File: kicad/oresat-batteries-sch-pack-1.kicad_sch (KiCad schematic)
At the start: 79 parts, among them Q12 SI7625DN-T1-GE3, Q13 SI7625DN-T1-GE3, Q14 NTR4101, Q15 NTR4101, Q16 SI7625DN-T1-GE3, Q17 SI7625DN-T1-GE3, Q18 SI7625DN-T1-GE3, Q19 SI7625DN-T1-GE3, Q6 PM45VEN, Q7 PM45VEN, Q8 PM45VEN, Q9 PM45VEN, U10 LTC4412, U11 LTC4412, U12 MAX17205G, U8 S-8209AAA-T8T1U, U9 S-8209AAA-T8T1U

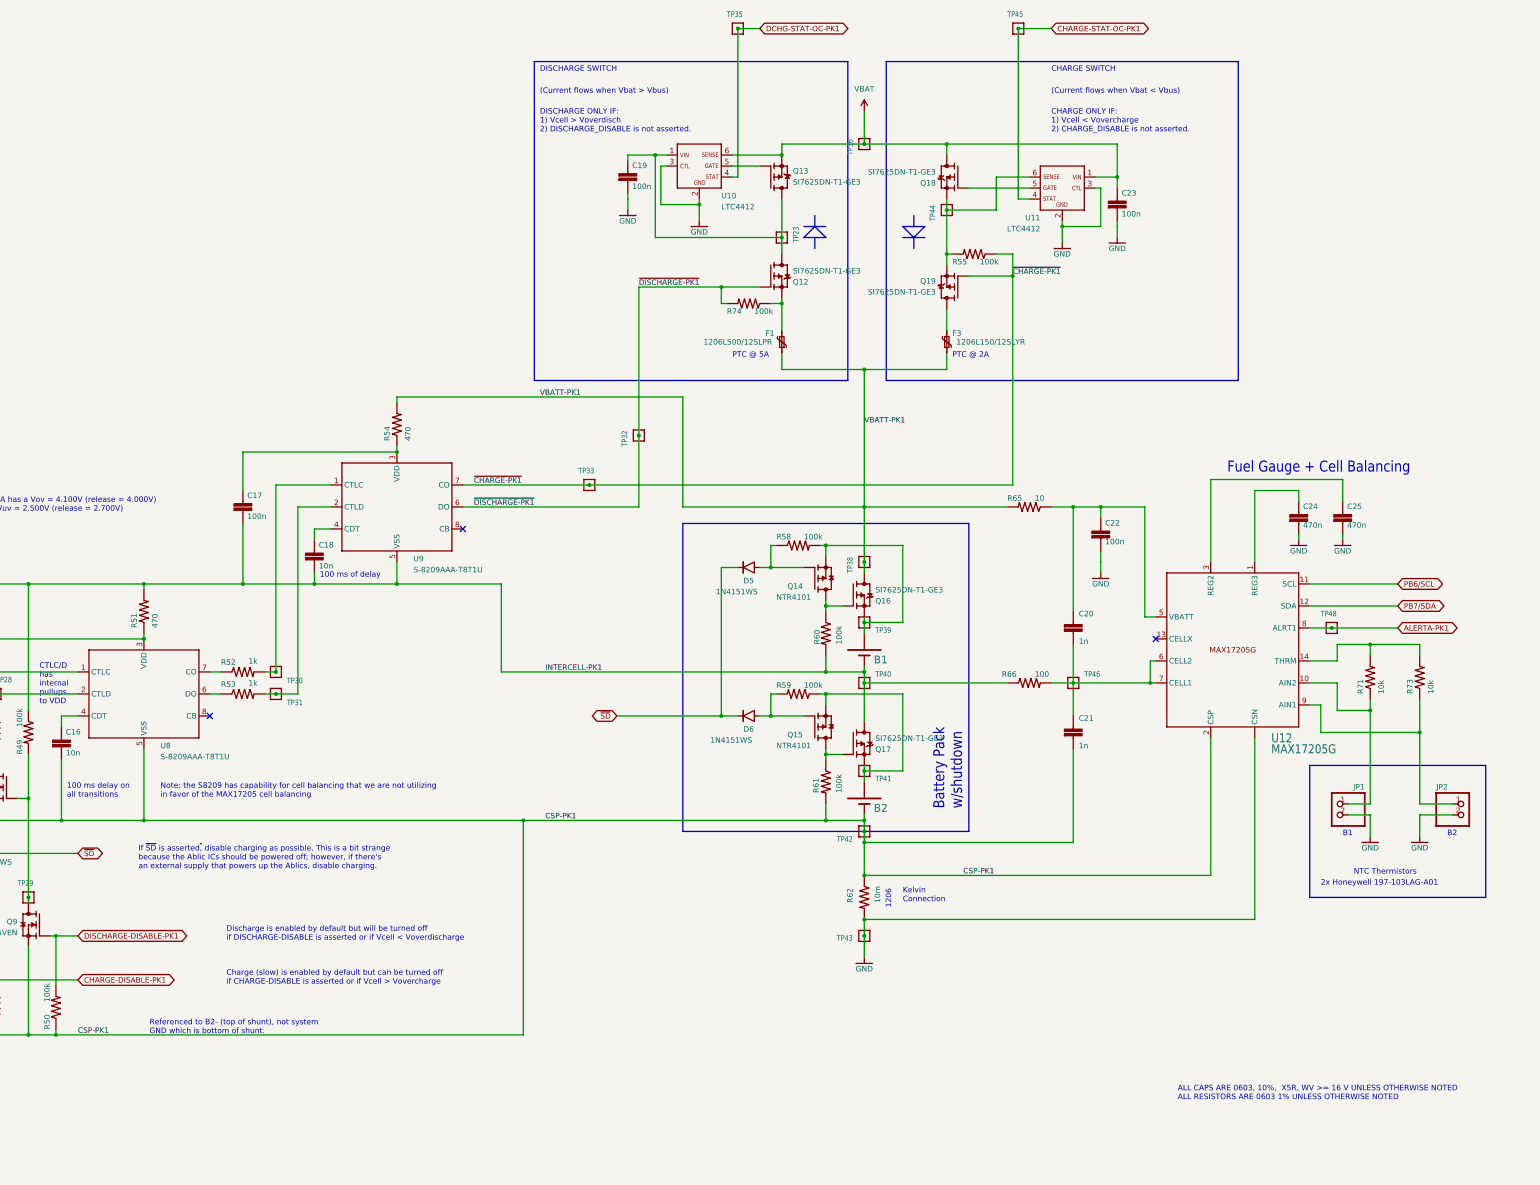
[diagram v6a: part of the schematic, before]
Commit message: Starting Battery Card 4.0
Changed root sheet to hierarchical sheet. No change to schematic or layout yet. Updated the stackup with oresat template. Switched to variables for version and date.
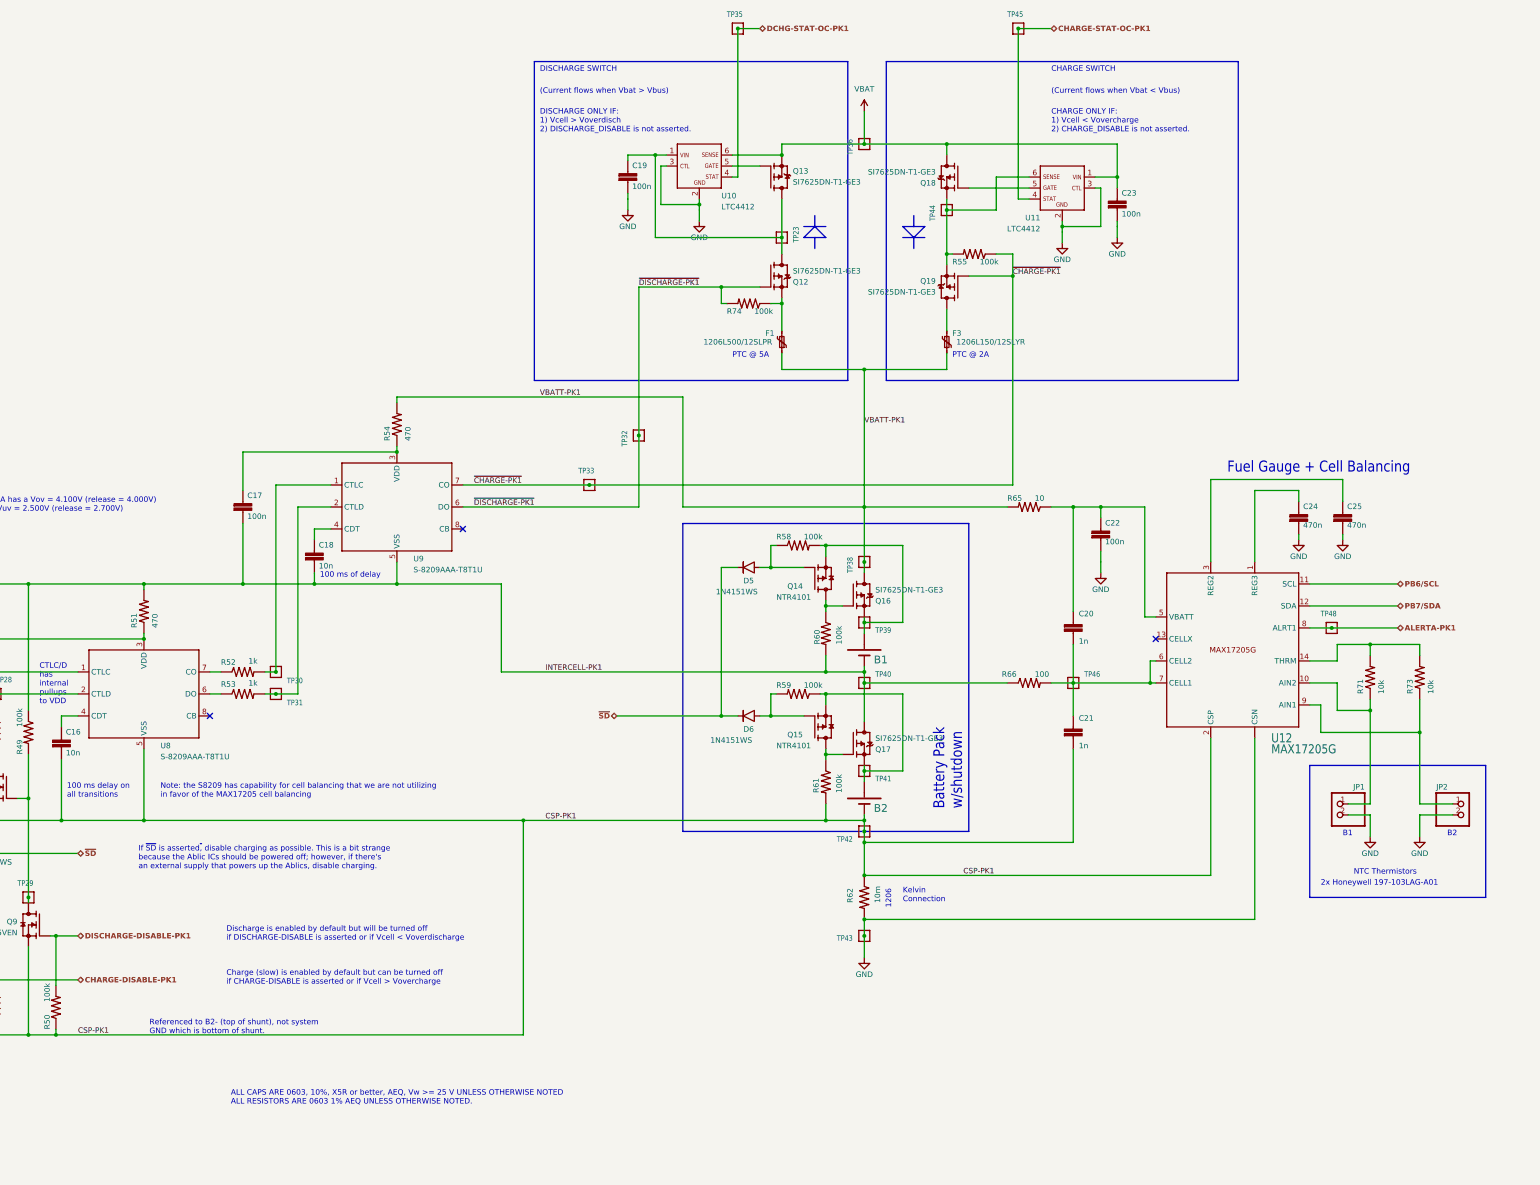
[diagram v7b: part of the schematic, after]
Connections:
- net PB6/SCL renamed PB6/SCL
- net PB7/SDA renamed PB7/SDA
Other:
- note added: "ALL CAPS ARE 0603, 10%, X5R or better, AEQ, Vw >= 25 V UNLESS OTHERWISE NOTED ALL RESISTORS ARE 0603 1% AEQ UNLESS OTHERWISE NOTED."
- company: (none) -> Portland State Aerospace Society
- title: OreSat Battery Card - Pack 1 (Bottom) -> OreSat Battery Card

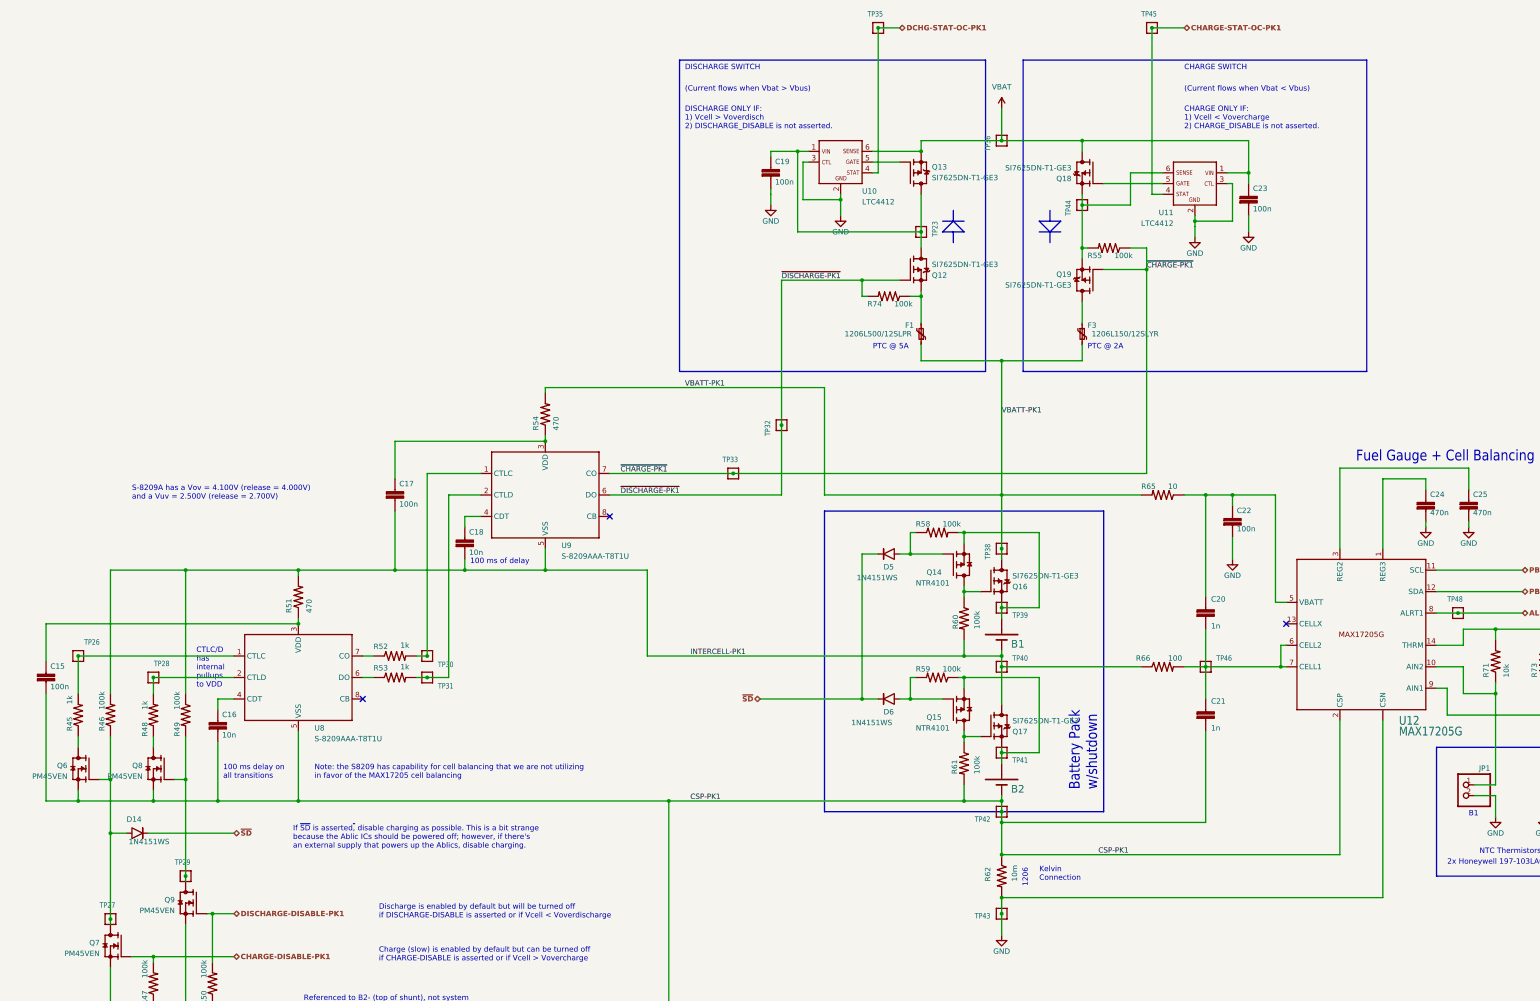
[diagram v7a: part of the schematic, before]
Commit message: Minor polishing, removing outdated OPD signals and OPD power jumper.
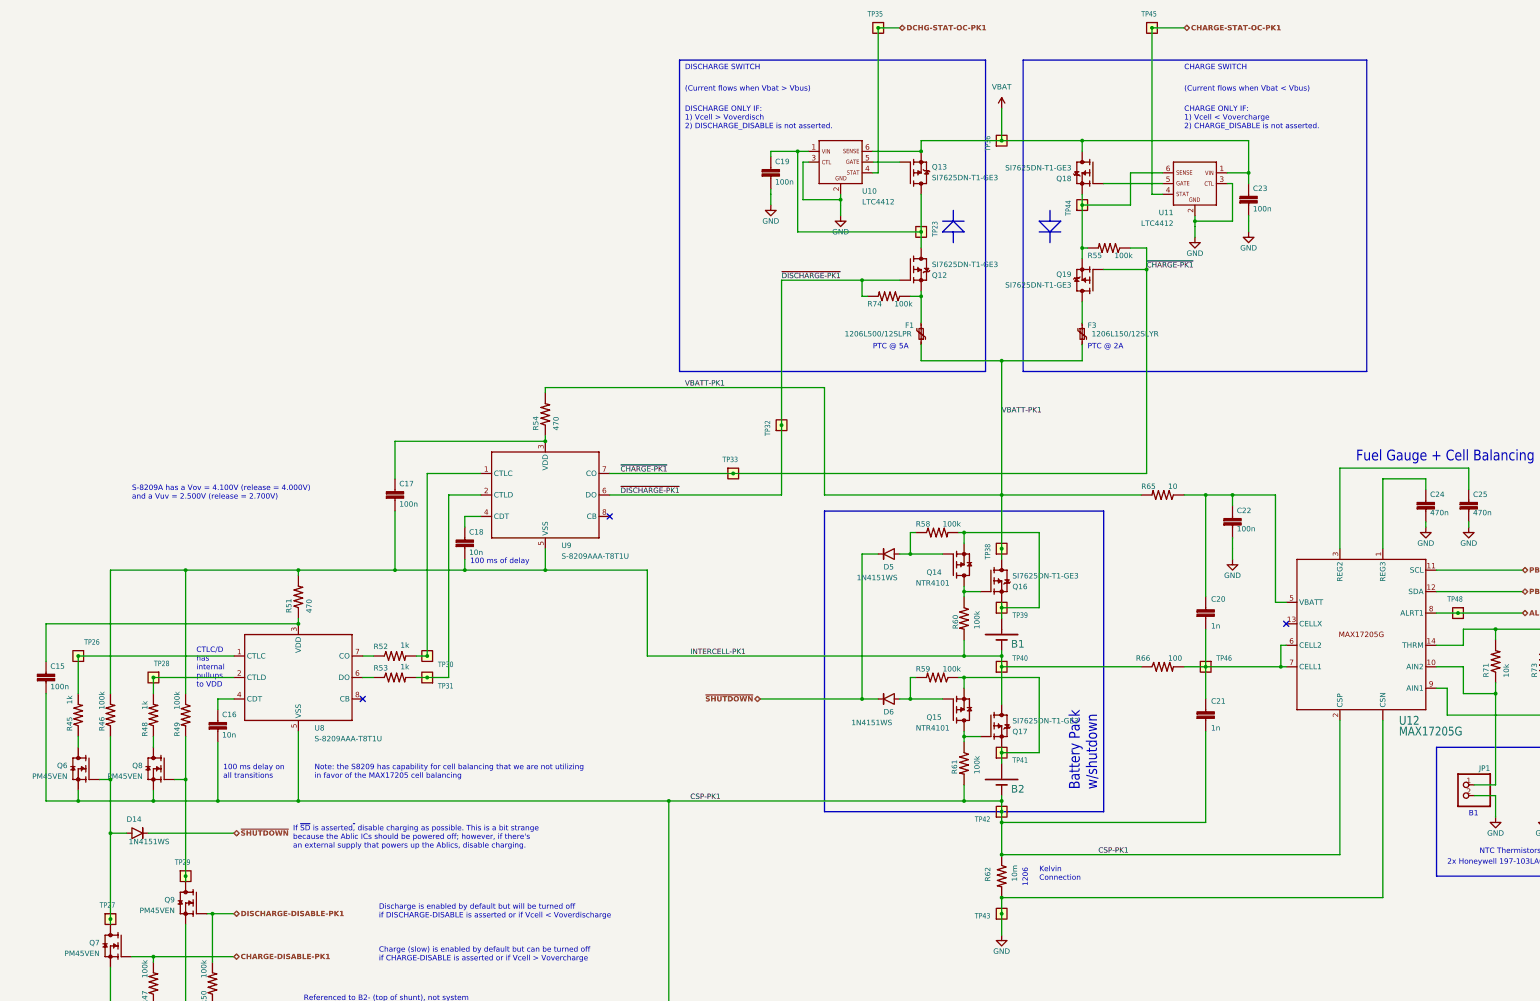
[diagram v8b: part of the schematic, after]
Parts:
- TP23, TP26, TP27, TP28, TP29, TP30, TP31, TP32, TP33, TP35, TP36, TP38, TP39, TP40, TP41, TP42, TP43, TP44, TP45, TP46, TP48: footprint oresat-batteries:1X01 -> oresat-misc:TestPoint-0.75mm-th; symbol oresat-batteries-eagle-import:TEST-POINT-LARGE-SQUARE -> oresat-misc:Test-Point-0.75mm-th; now left out of the parts list
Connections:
- net ~{SD} renamed ~{SHUTDOWN}
